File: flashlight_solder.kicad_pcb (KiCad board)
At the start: 2 copper layers, 58.4 x 25.4 mm, 7 parts, among them SW1 SW_Push

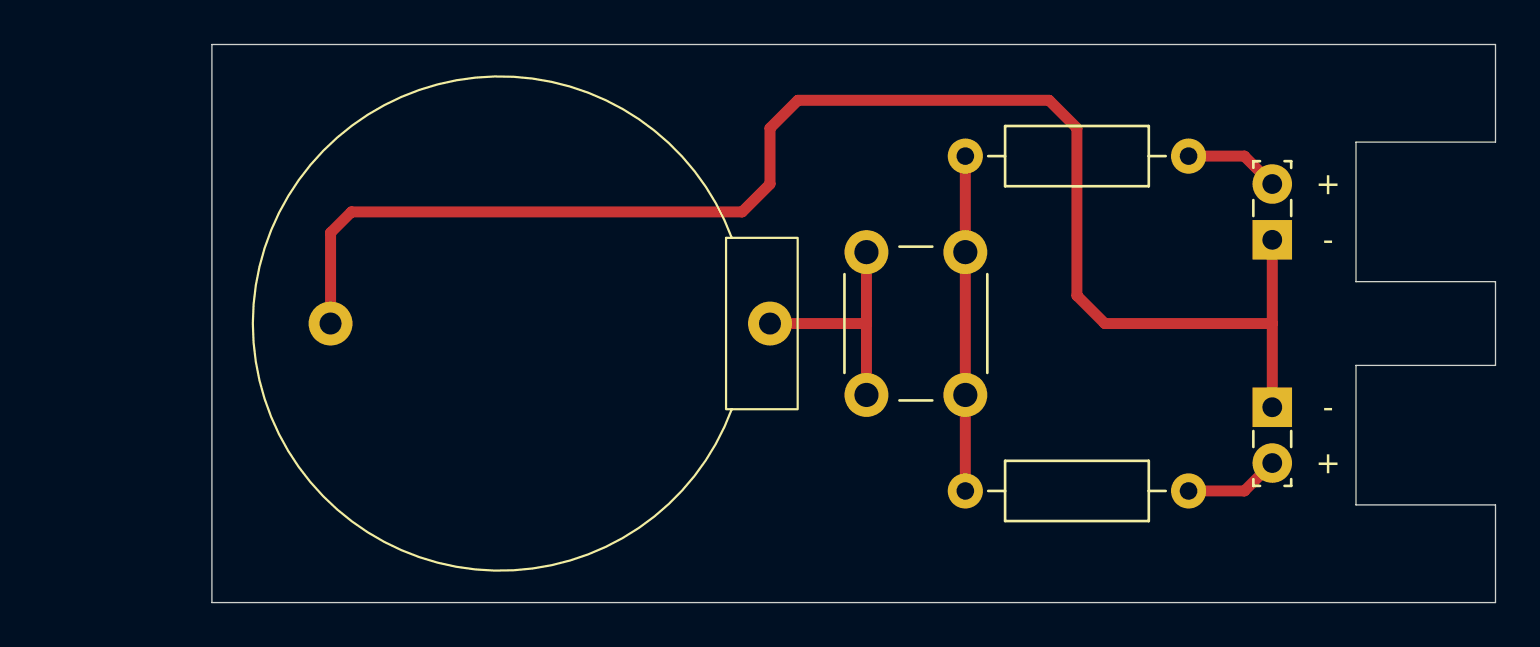
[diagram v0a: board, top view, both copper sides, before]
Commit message: Update board: - add keyhole - move button further front
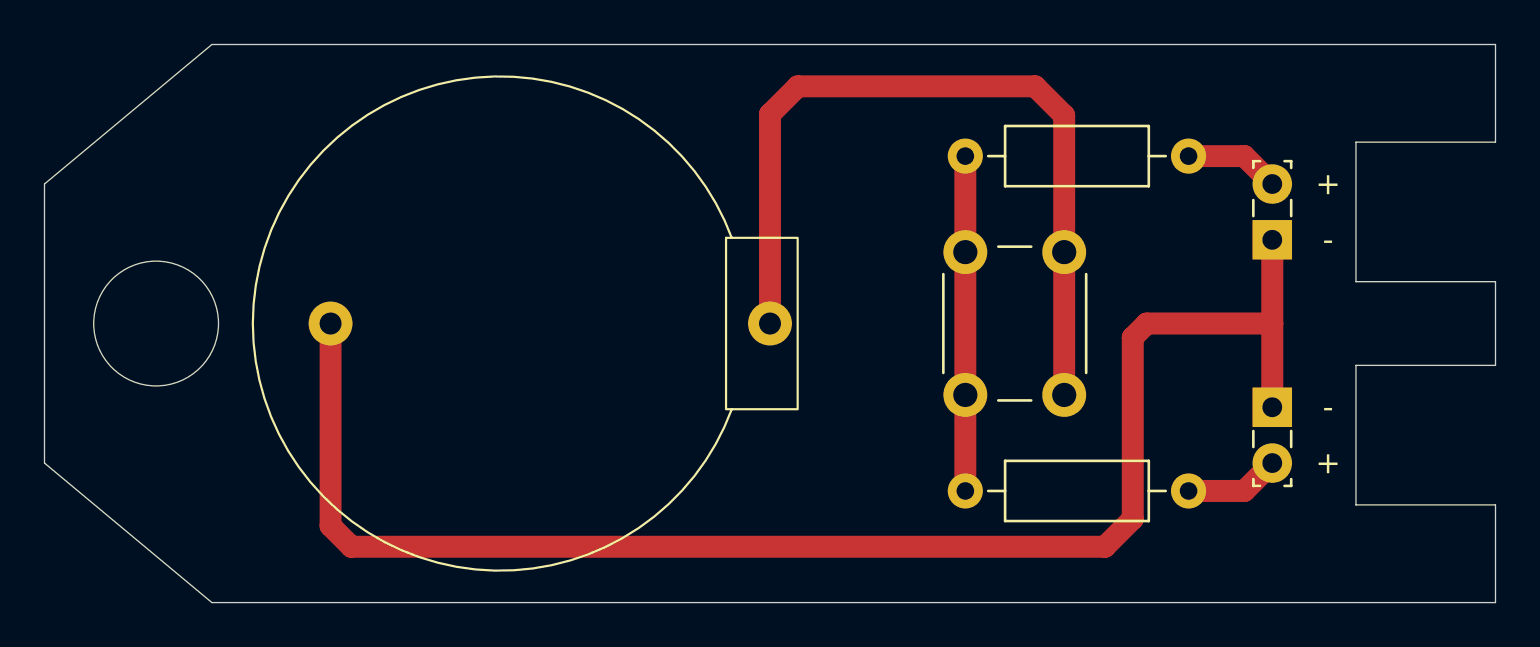
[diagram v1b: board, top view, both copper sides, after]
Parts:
- moved SW1 11.1 mm to (146.7, 92.0), turned to -90 degrees
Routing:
- net Net-(BT1-+): track 10.9 -> 36.7 mm
- net Net-(BT1--): track 67.3 -> 69.1 mm
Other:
- board size 58.4 x 25.4 mm -> 66 x 25.4 mm
- board text added: "CR2032 3V"

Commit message: Change to different battery holder part
- lower profile
- battery less likely to fall out
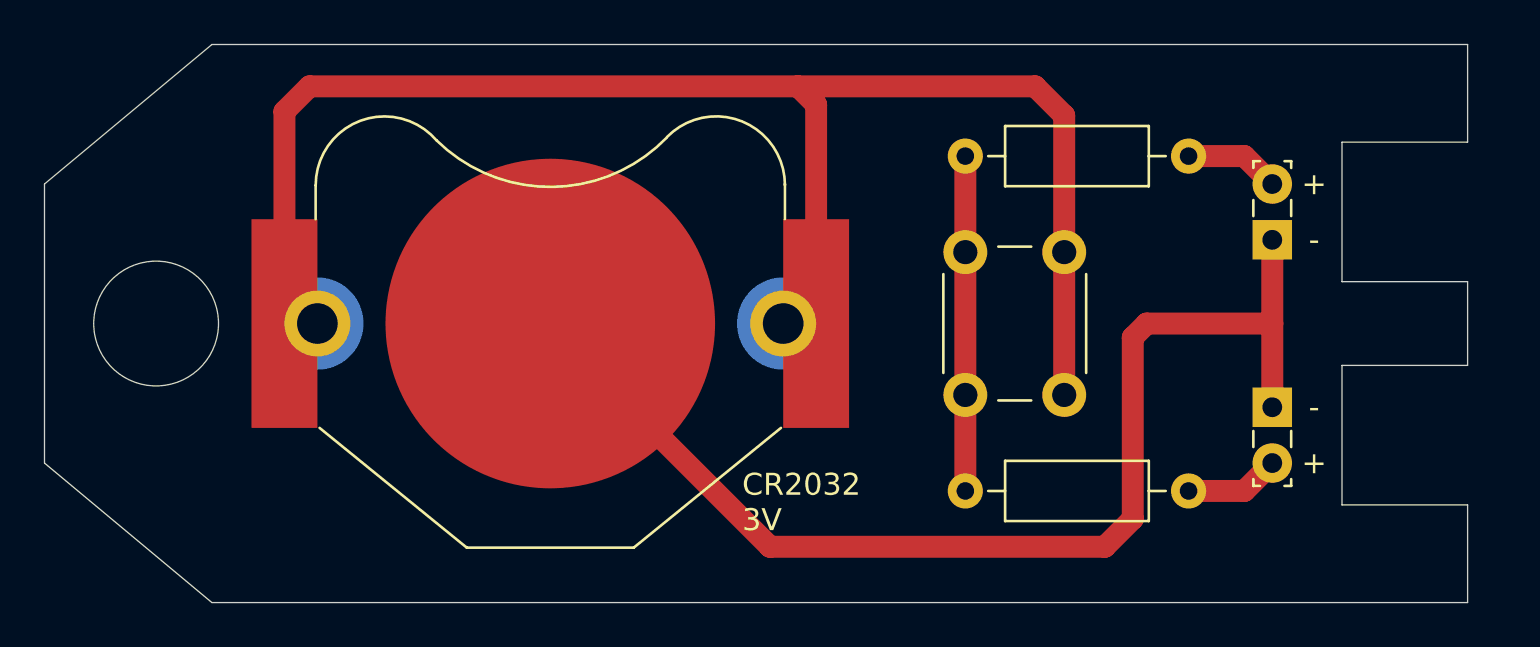
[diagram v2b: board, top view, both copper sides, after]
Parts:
- BT1: footprint fl-parts:CR2032-THT -> fl-parts:CR2032-THT-retainer
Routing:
- net Net-(BT1-+): track 36.7 -> 70.0 mm
- net Net-(BT1--): track 69.1 -> 53.8 mm
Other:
- board size 66 x 25.4 mm -> 64.8 x 25.4 mm
- board text added: "flashlight v1 by theamk"
- board text removed: "learn-to-solder flashlight v1 by theamk"
